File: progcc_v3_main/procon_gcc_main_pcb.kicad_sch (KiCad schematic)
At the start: 103 parts, among them J1 Rumble, J2 Rumble, J3 To Button Board, J4 Conn_01x06_Female, J5 Conn_01x02_Pin, J9 USB_C_Receptacle, Q1 Q_PMOS_GDS, Q2 Q_PMOS_GDS, Q3 Q_PMOS_GDS, Q4 BSS138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

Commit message: Update button board
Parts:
- added SW4: ~, progcc_v3:TS35CA, symbol progcc_v3:TS35CA
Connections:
- net GND: now also J9.S1 (SHIELD), SW4.1, SW4.3
- net MODE_BUTTON: now reaches U6.17 (GPIO14)
- net MODE_BUTTON: now also SW4.2
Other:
- note added: "Mode Button"
- moved on the sheet: R19, Y1

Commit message: Update part #
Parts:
- Y1: MPN (none) -> CSTNE12M0GH5L000R0
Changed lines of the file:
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@@
+      (effects (font (size 1.27 1.27)) hide)
+    )
+    (property "MPN" "CSTNE12M0GH5L000R0" (at 260.35 171.45 90)
       (effects (font (size 1.27 1.27)) hide)
     )

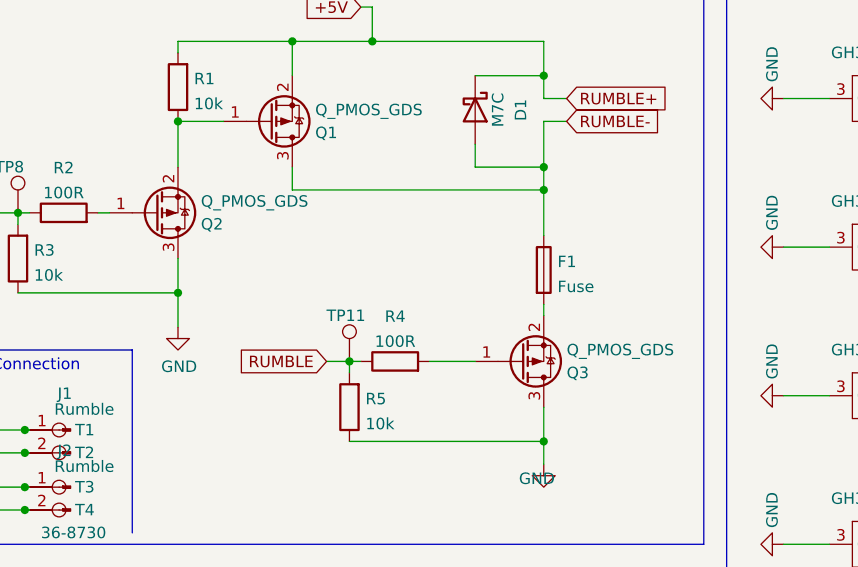
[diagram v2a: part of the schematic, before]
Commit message: Fixed missing trace
Missing trace and N Channel mosfet fix
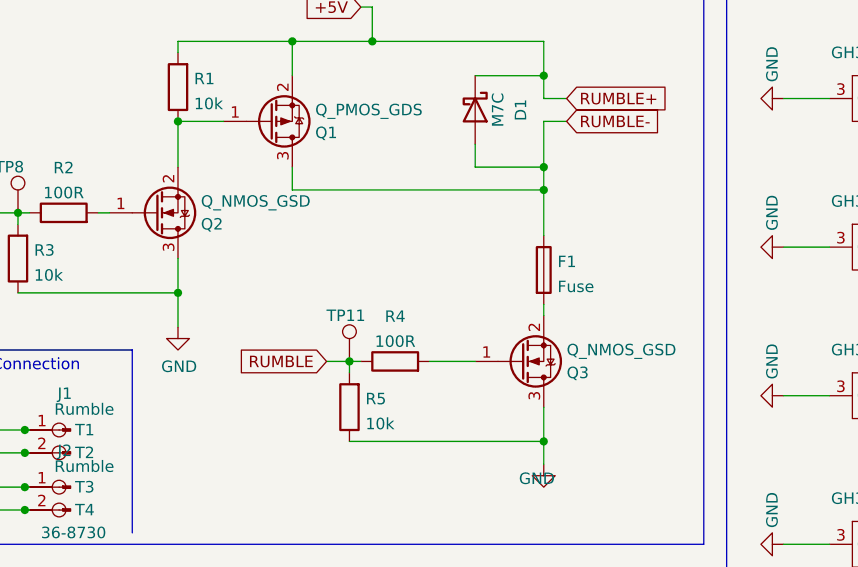
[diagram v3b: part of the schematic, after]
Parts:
- J9: footprint procon_gcc:Shou Han Type-C 24P QCHT -> progcc_v3:Shou Han Type-C 24P QCHT
- Q1: MPN (none) -> AO3401A
- Q2, Q3: value Q_PMOS_GDS -> Q_NMOS_GSD; symbol Device:Q_PMOS_GSD -> Device:Q_NMOS_GSD; LCSC C15127 -> C20917; MPN (none) -> AO3400A
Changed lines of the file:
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@@
       (effects (font (size 1.27 1.27)) hide)
     )
+    (property "MPN" "AO3401A" (at 119.38 35.56 0)
+      (effects (font (size 1.27 1.27)) hide)
+    )
+    (property "Field6" "" (at 119.38 35.56 0)
+      (effects (font (size 1.27 1.27)) hide)
+    )
     (pin "1")
     (pin "2")
@@
     )
   )
-  (symbol (lib_id "Device:Q_PMOS_GSD") (at 147.32 62.23 0) (mirror x) (unit 1)
+  (symbol (lib_id "Device:Q_NMOS_GSD") (at 147.32 62.23 0) (mirror x) (unit 1)
     (in_bom yes) (on_board yes) (dnp no)
     (property "Reference" "Q3" (at 152.4 63.5 0)
       (effects (font (size 1.27 1.27)) (justify left))
     )
-    (property "Value" "Q_PMOS_GDS" (at 152.4 60.96 0)
+    (property "Value" "Q_NMOS_GSD" (at 152.4 60.96 0)
       (effects (font (size 1.27 1.27)) (justify left))
     )
-    (property "Footprint" "Package_TO_SOT_SMD:SOT-23" (at 130.81 67.31 0)
+    (property "Footprint" "Package_TO_SOT_SMD:SOT-23" (at 152.4 64.77 0)
       (effects (font (size 1.27 1.27)) hide)
     )
@@
       (effects (font (size 1.27 1.27)) hide)
     )
-    (property "LCSC" "C15127" (at 128.27 69.85 0)
+    (property "LCSC" "C20917" (at 128.27 69.85 0)
+      (effects (font (size 1.27 1.27)) hide)
+    )
+    (property "MPN" "AO3400A" (at 147.32 62.23 0)
       (effects (font (size 1.27 1.27)) hide)
     )
@@
       (effects (font (size 1.27 1.27)))
     )
-    (property "Footprint" "procon_gcc:Shou Han Type-C 24P QCHT" (at 33.02 143.51 0)
+    (property "Footprint" "progcc_v3:Shou Han Type-C 24P QCHT" (at 33.02 143.51 0)
       (effects (font (size 1.27 1.27)) hide)
     )
@@
     )
   )
-  (symbol (lib_id "Device:Q_PMOS_GSD") (at 106.68 45.72 0) (mirror x) (unit 1)
+  (symbol (lib_id "Device:Q_NMOS_GSD") (at 106.68 45.72 0) (mirror x) (unit 1)
     (in_bom yes) (on_board yes) (dnp no)
     (property "Reference" "Q2" (at 111.76 46.99 0)
       (effects (font (size 1.27 1.27)) (justify left))
     )
-    (property "Value" "Q_PMOS_GDS" (at 111.76 44.45 0)
+    (property "Value" "Q_NMOS_GSD" (at 111.76 44.45 0)
       (effects (font (size 1.27 1.27)) (justify left))
     )
-    (property "Footprint" "Package_TO_SOT_SMD:SOT-23" (at 90.17 50.8 0)
+    (property "Footprint" "Package_TO_SOT_SMD:SOT-23" (at 111.76 48.26 0)
       (effects (font (size 1.27 1.27)) hide)
     )
@@
       (effects (font (size 1.27 1.27)) hide)
     )
-    (property "LCSC" "C15127" (at 87.63 53.34 0)
+    (property "LCSC" "C20917" (at 87.63 53.34 0)
+      (effects (font (size 1.27 1.27)) hide)
+    )
+    (property "MPN" "AO3400A" (at 106.68 45.72 0)
       (effects (font (size 1.27 1.27)) hide)
     )

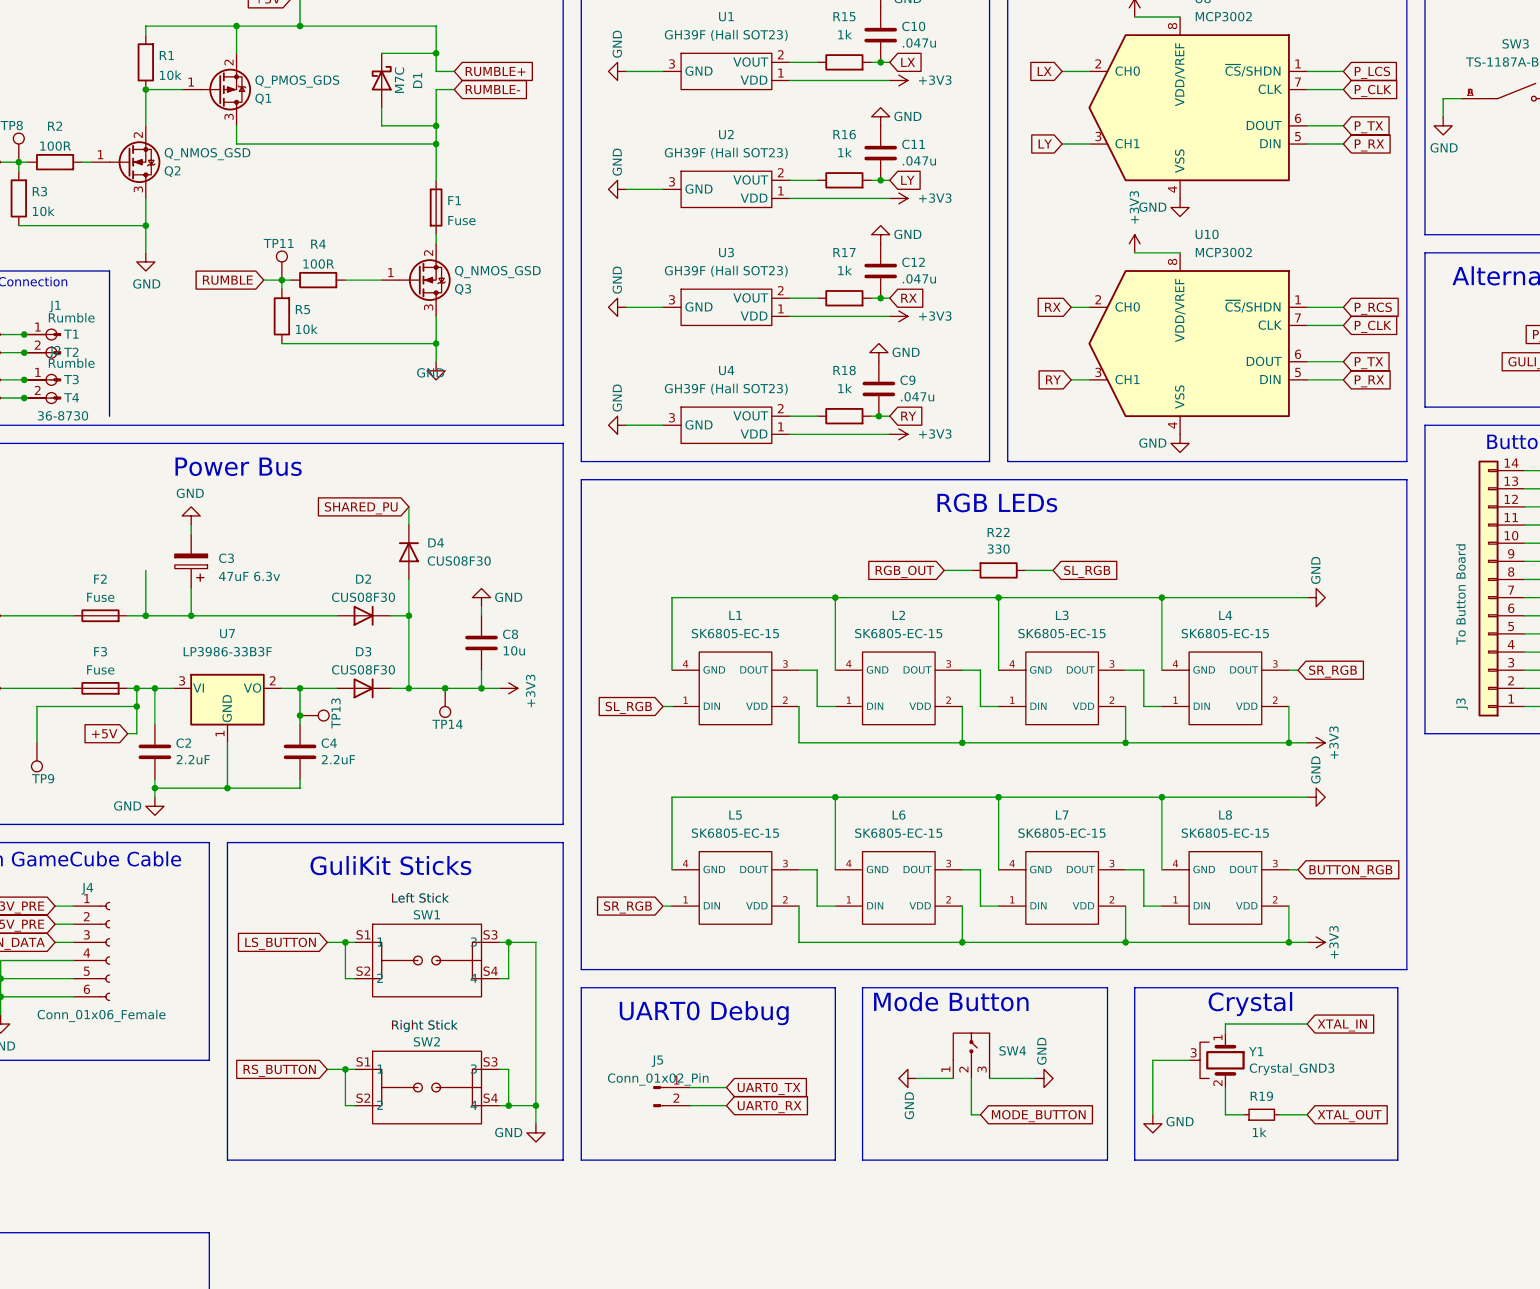
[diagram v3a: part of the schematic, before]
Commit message: Update proto
- Update stick position
- Adjust some screw position slightly
- Fix schematic for Crystal and Rumble
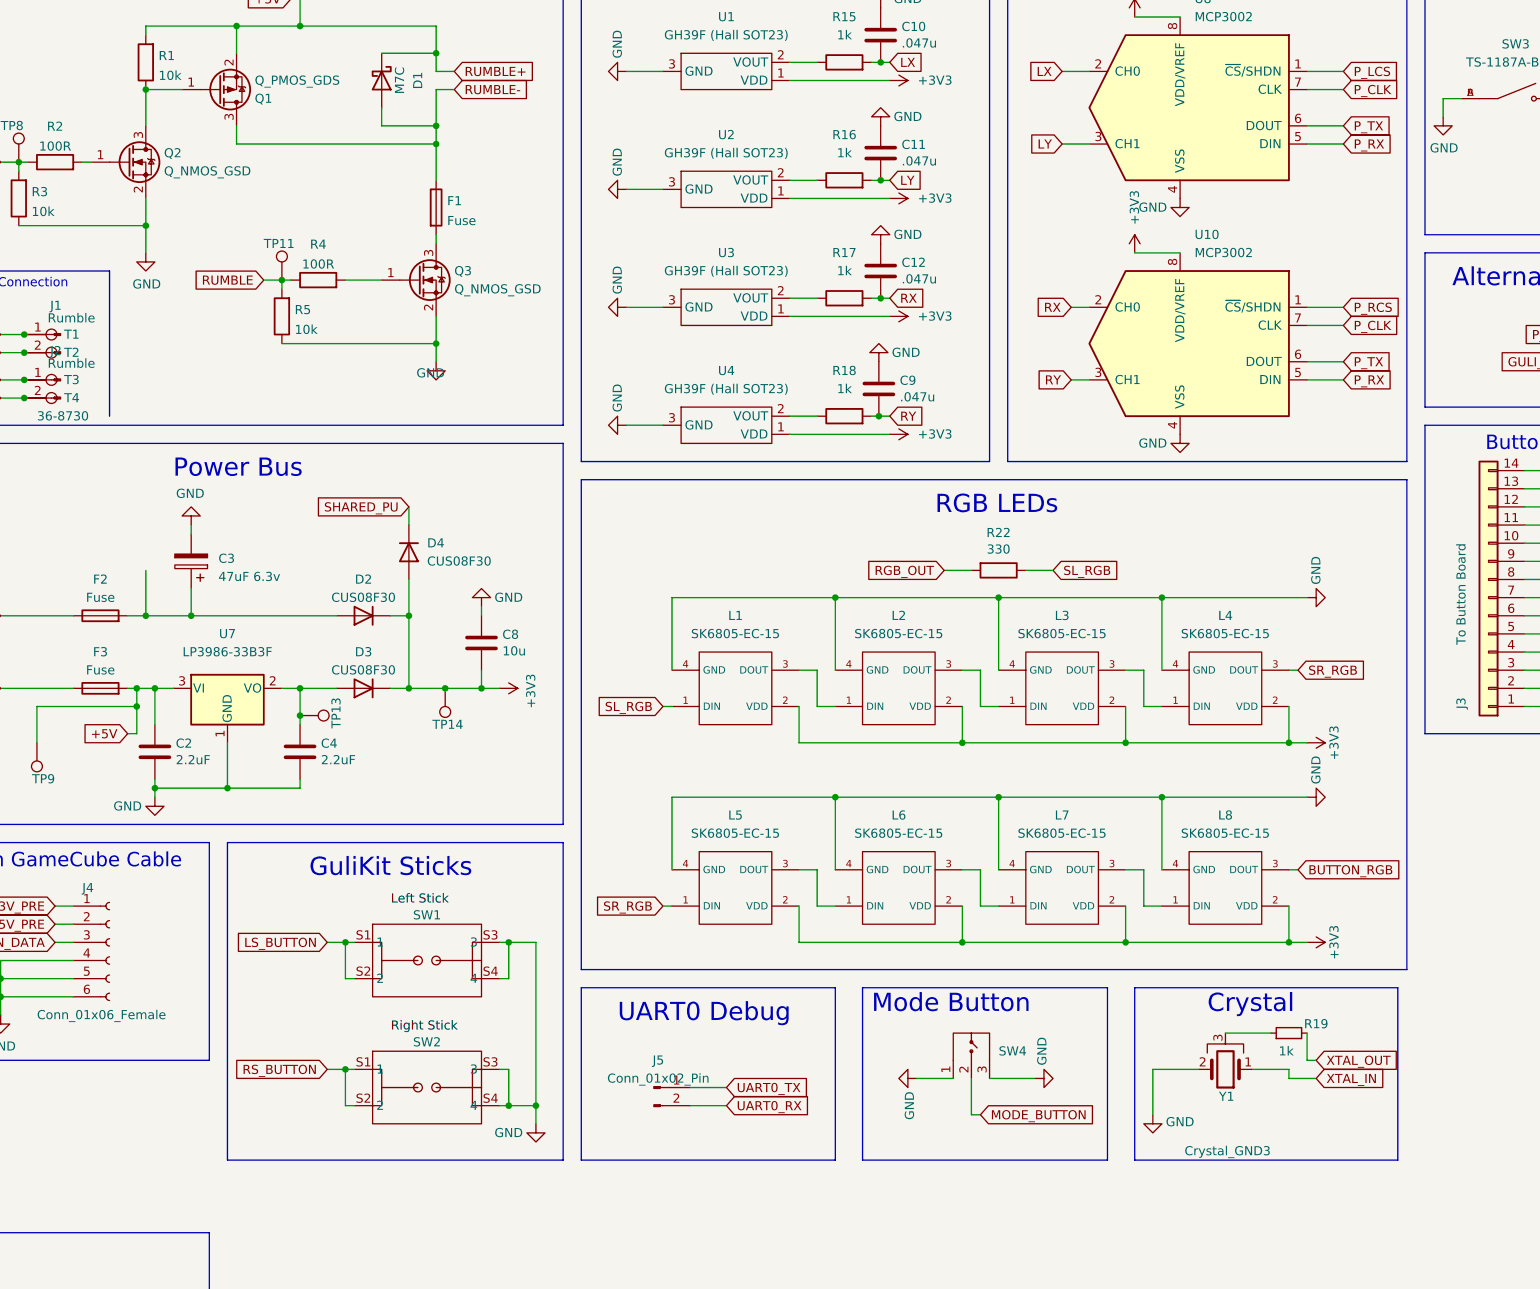
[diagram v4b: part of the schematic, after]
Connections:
- net GND: now also Q2.2 (S), Q3.2 (S), Y1.2; no longer Q2.3 (D), Q3.3 (D), Y1.3
- net at Q1.1 (G), R1.1: now also Q2.3 (D); no longer Q2.2 (S)
- net at R19.1: now also Y1.3; no longer Y1.2
- net at F1.2: now also Q3.3 (D); no longer Q3.2 (S)
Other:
- moved on the sheet: R19, Y1
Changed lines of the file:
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@@
     (stroke (width 0) (type default))
   )
+  (wire (pts (xy 269.24 173.99) (xy 273.05 173.99))
+    (stroke (width 0) (type default))
+  )
   (wire (pts (xy 394.97 168.91) (xy 400.05 168.91))
     (stroke (width 0) (type default))
@@
     (stroke (width 0) (type default))
   )
+  (wire (pts (xy 250.19 172.72) (xy 256.54 172.72))
+    (stroke (width 0) (type default))
+  )
   (polyline (pts (xy 73.66 13.97) (xy 73.66 105.41))
     (stroke (width 0) (type default))
@@
     (stroke (width 0) (type default))
   )
+  (wire (pts (xy 264.16 172.72) (xy 269.24 172.72))
+    (stroke (width 0) (type default))
+  )
   (wire (pts (xy 35.56 21.59) (xy 35.56 25.4))
     (stroke (width 0) (type default))
@@
     (stroke (width 0) (type default))
   )
+  (wire (pts (xy 271.78 171.45) (xy 273.05 171.45))
+    (stroke (width 0) (type default))
+  )
   (wire (pts (xy 205.74 106.68) (xy 205.74 116.84))
     (stroke (width 0) (type default))
@@
     (stroke (width 0) (type default))
   )
-  (wire (pts (xy 260.35 179.07) (xy 262.89 179.07))
+  (wire (pts (xy 260.35 167.64) (xy 266.7 167.64))
     (stroke (width 0) (type default))
   )
@@
     (stroke (width 0) (type default))
   )
-  (wire (pts (xy 255.27 171.45) (xy 250.19 171.45))
-    (stroke (width 0) (type default))
-  )
   (wire (pts (xy 379.73 127) (xy 382.27 127))
     (stroke (width 0) (type default))
@@
     (stroke (width 0) (type default))
   )
-  (wire (pts (xy 267.97 179.07) (xy 271.78 179.07))
-    (stroke (width 0) (type default))
-  )
   (wire (pts (xy 60.96 220.98) (xy 66.04 220.98))
     (stroke (width 0) (type default))
@@
     (stroke (width 0) (type default))
   )
-  (wire (pts (xy 260.35 167.64) (xy 260.35 166.37))
-    (stroke (width 0) (type default))
-  )
   (wire (pts (xy 210.82 31.75) (xy 212.09 31.75))
     (stroke (width 0) (type default))
@@
     (stroke (width 0) (type default))
   )
+  (wire (pts (xy 269.24 172.72) (xy 269.24 173.99))
+    (stroke (width 0) (type default))
+  )
   (wire (pts (xy 142.24 30.48) (xy 149.86 30.48))
     (stroke (width 0) (type default))
@@
     (stroke (width 0) (type default))
   )
-  (wire (pts (xy 260.35 166.37) (xy 271.78 166.37))
-    (stroke (width 0) (type default))
-  )
   (wire (pts (xy 355.6 25.4) (xy 355.6 29.21))
     (stroke (width 0) (type default))
@@
     (stroke (width 0) (type default))
   )
+  (wire (pts (xy 271.78 167.64) (xy 271.78 171.45))
+    (stroke (width 0) (type default))
+  )
   (wire (pts (xy 217.17 173.99) (xy 222.25 173.99))
     (stroke (width 0) (type default))
@@
     (stroke (width 0) (type default))
   )
-  (wire (pts (xy 250.19 171.45) (xy 250.19 179.07))
+  (wire (pts (xy 250.19 172.72) (xy 250.19 179.07))
     (stroke (width 0) (type default))
   )
@@
     (stroke (width 0) (type default))
   )
-  (wire (pts (xy 260.35 175.26) (xy 260.35 179.07))
-    (stroke (width 0) (type default))
-  )
   (wire (pts (xy 149.86 40.64) (xy 149.86 35.56))
     (stroke (width 0) (type default))
@@
     )
   )
-  (global_label "XTAL_OUT" (shape input) (at 271.78 179.07 0) (fields_autoplaced)
+  (global_label "XTAL_OUT" (shape input) (at 273.05 171.45 0) (fields_autoplaced)
     (effects (font (size 1.27 1.27)) (justify left))
-    (property "Intersheetrefs" "${INTERSHEET_REFS}" (at 283.0831 179.1494 0)
+    (property "Intersheetrefs" "${INTERSHEET_REFS}" (at 284.3531 171.5294 0)
       (effects (font (size 1.27 1.27)) (justify left) hide)
     )
@@
     )
   )
-  (global_label "XTAL_IN" (shape input) (at 271.78 166.37 0) (fields_autoplaced)
+  (global_label "XTAL_IN" (shape input) (at 273.05 173.99 0) (fields_autoplaced)
     (effects (font (size 1.27 1.27)) (justify left))
-    (property "Intersheetrefs" "${INTERSHEET_REFS}" (at 281.3898 166.4494 0)
+    (property "Intersheetrefs" "${INTERSHEET_REFS}" (at 282.6598 174.0694 0)
       (effects (font (size 1.27 1.27)) (justify left) hide)
     )
@@
     )
   )
-  (symbol (lib_id "Device:Crystal_GND3") (at 260.35 171.45 270) (unit 1)
+  (symbol (lib_id "Device:Crystal_GND3") (at 260.35 172.72 180) (unit 1)
     (in_bom yes) (on_board yes) (dnp no)
-    (property "Reference" "Y1" (at 263.652 170.2816 90)
+    (property "Reference" "Y1" (at 261.62 176.53 0)
       (effects (font (size 1.27 1.27)) (justify left))
     )
-    (property "Value" "Crystal_GND3" (at 263.652 172.593 90)
+    (property "Value" "Crystal_GND3" (at 266.7 184.15 0)
       (effects (font (size 1.27 1.27)) (justify left))
     )
-    (property "Footprint" "Crystal:Resonator_SMD_Murata_CSTxExxV-3Pin_3.0x1.1mm" (at 260.35 171.45 0)
+    (property "Footprint" "Crystal:Resonator_SMD_Murata_CSTxExxV-3Pin_3.0x1.1mm" (at 260.35 172.72 0)
       (effects (font (size 1.27 1.27)) hide)
     )
-    (property "Datasheet" "~" (at 260.35 171.45 0)
+    (property "Datasheet" "~" (at 260.35 172.72 0)
       (effects (font (size 1.27 1.27)) hide)
     )
-    (property "MPN" "CSTNE12M0GH5L000R0" (at 260.35 171.45 90)
+    (property "MPN" "CSTNE12M0GH5L000R0" (at 260.35 172.72 90)
       (effects (font (size 1.27 1.27)) hide)
     )
@@
     )
   )
-  (symbol (lib_id "Device:Q_NMOS_GSD") (at 147.32 62.23 0) (mirror x) (unit 1)
+  (symbol (lib_id "Device:Q_NMOS_GSD") (at 147.32 62.23 0) (unit 1)
     (in_bom yes) (on_board yes) (dnp no)
-    (property "Reference" "Q3" (at 152.4 63.5 0)
+    (property "Reference" "Q3" (at 152.4 60.96 0)
       (effects (font (size 1.27 1.27)) (justify left))
     )
-    (property "Value" "Q_NMOS_GSD" (at 152.4 60.96 0)
+    (property "Value" "Q_NMOS_GSD" (at 152.4 63.5 0)
       (effects (font (size 1.27 1.27)) (justify left))
     )
-    (property "Footprint" "Package_TO_SOT_SMD:SOT-23" (at 152.4 64.77 0)
+    (property "Footprint" "Package_TO_SOT_SMD:SOT-23" (at 152.4 59.69 0)
       (effects (font (size 1.27 1.27)) hide)
     )
@@
       (effects (font (size 1.27 1.27)) hide)
     )
-    (property "LCSC" "C20917" (at 128.27 69.85 0)
+    (property "LCSC" "C20917" (at 128.27 54.61 0)
       (effects (font (size 1.27 1.27)) hide)
     )
@@
     )
   )
-  (symbol (lib_id "Device:R_Small") (at 265.43 179.07 90) (unit 1)
+  (symbol (lib_id "Device:R_Small") (at 269.24 167.64 90) (unit 1)
     (in_bom yes) (on_board yes) (dnp no)
-    (property "Reference" "R19" (at 265.43 176.53 90)
+    (property "Reference" "R19" (at 273.05 166.37 90)
       (effects (font (size 1.27 1.27)))
     )
-    (property "Value" "1k" (at 265.049 181.61 90)
+    (property "Value" "1k" (at 268.859 170.18 90)
       (effects (font (size 1.27 1.27)))
     )
-    (property "Footprint" "Resistor_SMD:R_0402_1005Metric" (at 265.43 179.07 0)
+    (property "Footprint" "Resistor_SMD:R_0402_1005Metric" (at 269.24 167.64 0)
       (effects (font (size 1.27 1.27)) hide)
     )
-    (property "Datasheet" "~" (at 265.43 179.07 0)
+    (property "Datasheet" "~" (at 269.24 167.64 0)
       (effects (font (size 1.27 1.27)) hide)
     )
@@
     )
   )
-  (symbol (lib_id "Device:Q_NMOS_GSD") (at 106.68 45.72 0) (mirror x) (unit 1)
+  (symbol (lib_id "Device:Q_NMOS_GSD") (at 106.68 45.72 0) (unit 1)
     (in_bom yes) (on_board yes) (dnp no)
-    (property "Reference" "Q2" (at 111.76 46.99 0)
+    (property "Reference" "Q2" (at 111.76 44.45 0)
       (effects (font (size 1.27 1.27)) (justify left))
     )
-    (property "Value" "Q_NMOS_GSD" (at 111.76 44.45 0)
+    (property "Value" "Q_NMOS_GSD" (at 111.76 46.99 0)
       (effects (font (size 1.27 1.27)) (justify left))
     )
-    (property "Footprint" "Package_TO_SOT_SMD:SOT-23" (at 111.76 48.26 0)
+    (property "Footprint" "Package_TO_SOT_SMD:SOT-23" (at 111.76 43.18 0)
       (effects (font (size 1.27 1.27)) hide)
     )
@@
       (effects (font (size 1.27 1.27)) hide)
     )
-    (property "LCSC" "C20917" (at 87.63 53.34 0)
+    (property "LCSC" "C20917" (at 87.63 38.1 0)
       (effects (font (size 1.27 1.27)) hide)
     )
